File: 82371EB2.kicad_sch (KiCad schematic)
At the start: 38 parts, among them Q5 2N7000, Q6 2N7000, Q8 2N7000, U17 74HC10, U23 82371EB, U27 74HC112, U28 74F07, U5 74LVC14, Y2 32.768KHz

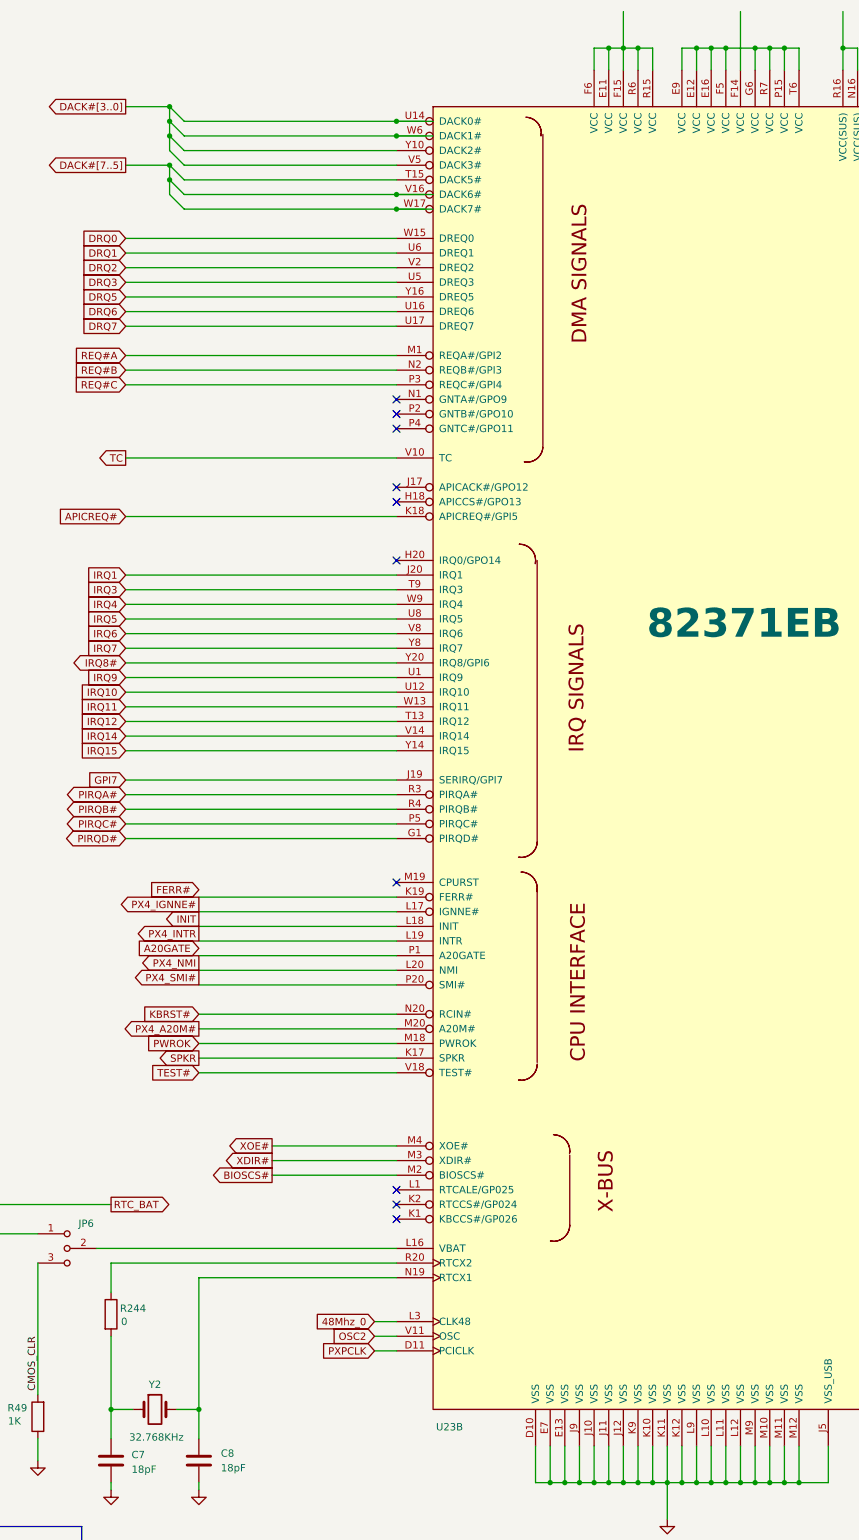
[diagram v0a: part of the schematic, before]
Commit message: page 6,7,8 82443BX chipset, various small fixes
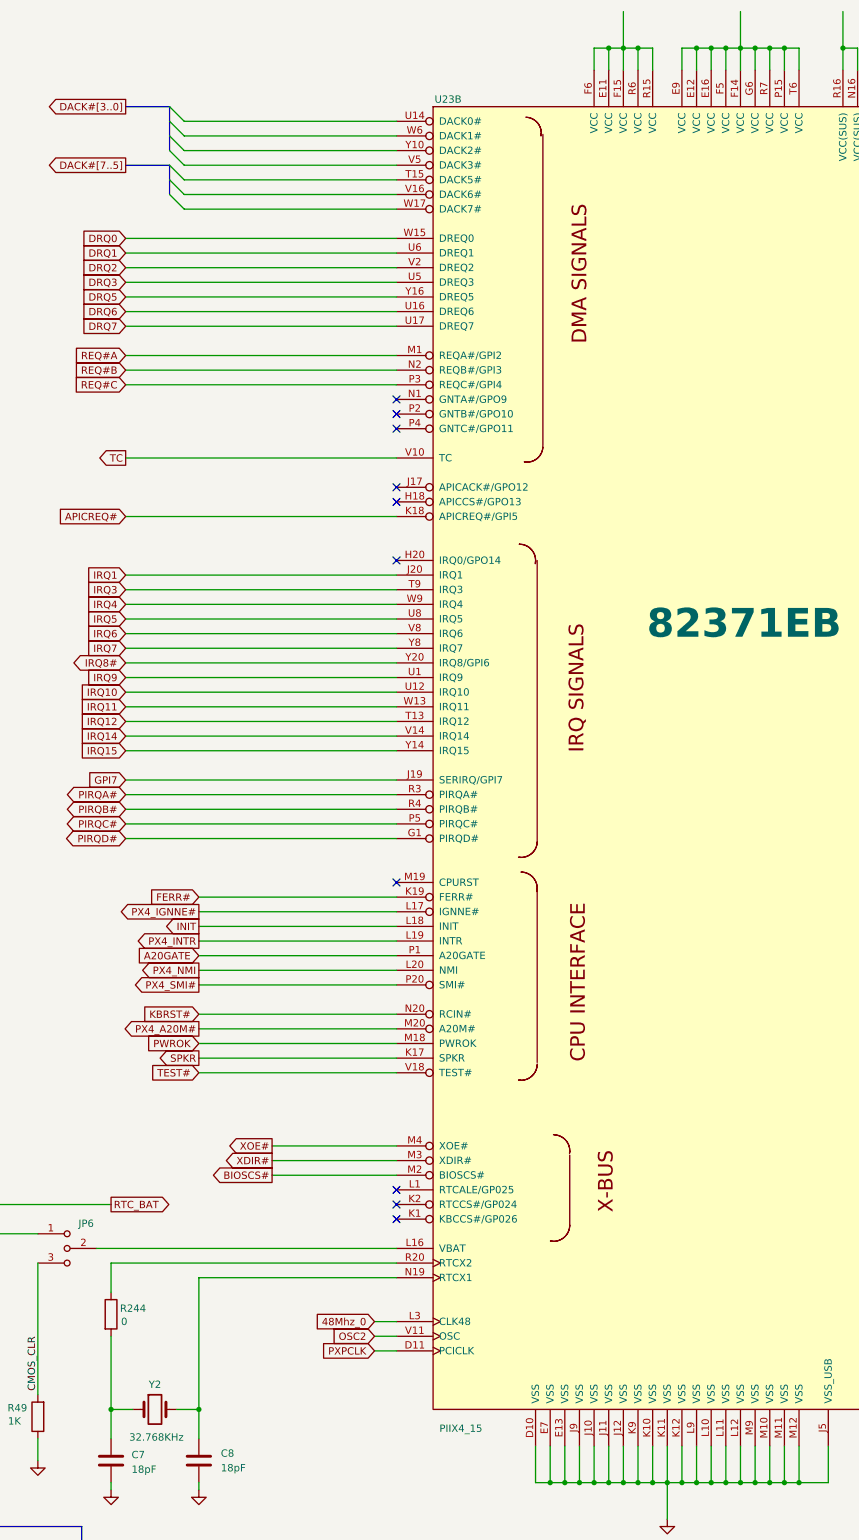
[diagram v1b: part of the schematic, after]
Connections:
- net A20GATE: now also U23.P1 (A20GATE)
- net DACK#[3..0]: no longer U23.U14 (DACK0#), U23.V5 (DACK3#), U23.W6 (DACK1#), U23.Y10 (DACK2#)
- net DACK#[7..5]: no longer U23.T15 (DACK5#), U23.V16 (DACK6#), U23.W17 (DACK7#)
- net FERR#: now also U23.K19 (FERR#)
- net INIT: now also U23.L18 (INIT)
- net PX4_IGNNE#: now also U23.L17 (IGNNE#)
- net PX4_INTR: now also U23.L19 (INTR)
- net PX4_NMI: now also U23.L20 (NMI)
- net PX4_SMI#: now also U23.P20 (SMI#)
- net at U23.E12 (VCC), U23.E16 (VCC), U23.E9 (VCC)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: now also U23.F14 (VCC)
